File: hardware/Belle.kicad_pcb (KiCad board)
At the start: 2 copper layers, 44.4 x 44.5 mm, 24 parts, among them P1 Bell CONN, P2 Battery CONN, P3 FTDI Flashing CONN, P4 Boot JUMPER, U1 74AHC1G14, U2 ESP-12, U3 AP2112

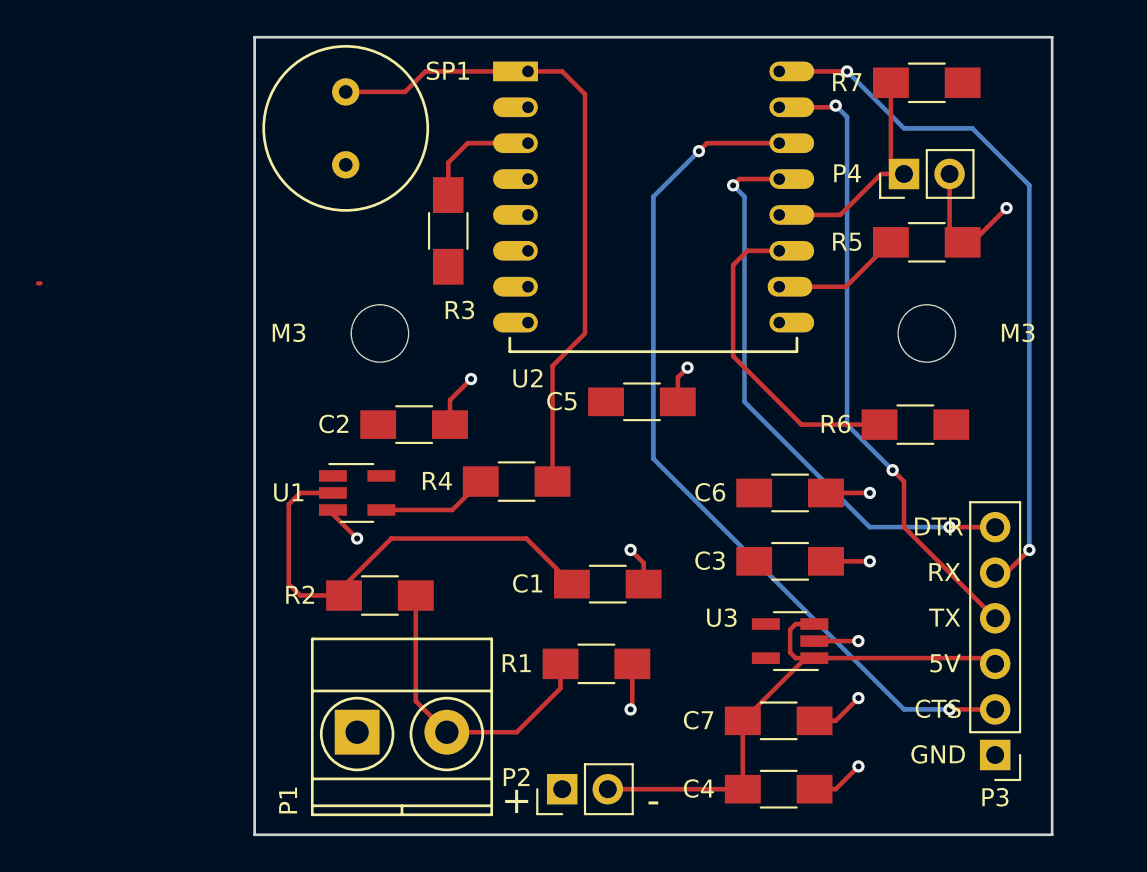
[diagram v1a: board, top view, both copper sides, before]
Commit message: add board info on the silkscreen. close #16
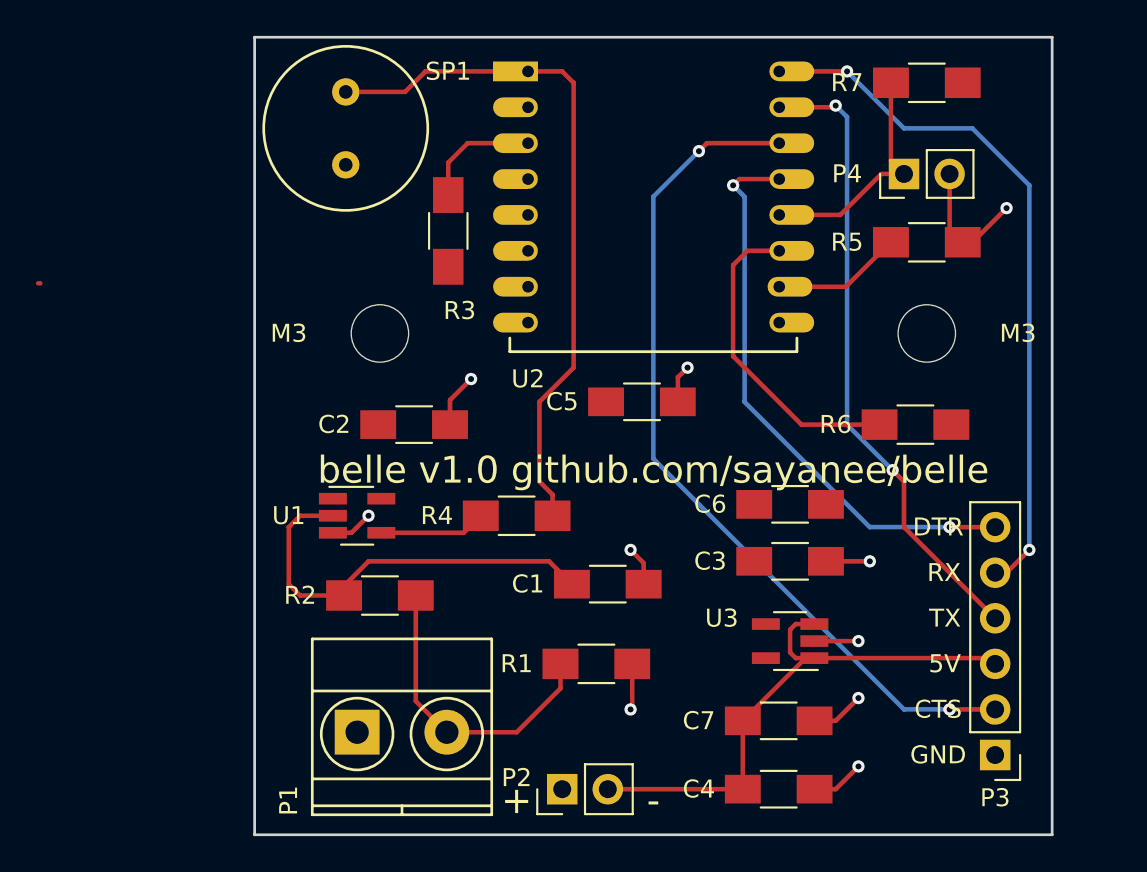
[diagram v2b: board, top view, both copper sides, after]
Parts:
- moved R4 1.91 mm to (167.0, 110.5)
- moved U1 1.27 mm to (158.1, 110.5)
- moved C6 0.64 mm to (182.2, 109.9)
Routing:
- net GND: track 33.5 -> 31.2 mm, vias 11 -> 10
- net Net-(R4-Pad1): track 36.7 -> 38.7 mm
- net Net-(C1-Pad1): track 25.3 -> 23.7 mm
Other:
- board text added: "belle v1.0 github.com/sayanee/belle"
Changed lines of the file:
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@@
   (general
     (links 46)
-    (no_connects 0)
+    (no_connects 1)
     (area 139.955999 76.695999 196.925001 128.345001)
     (thickness 1.6)
-    (drawings 12)
-    (tracks 123)
+    (drawings 13)
+    (tracks 124)
     (zones 0)
     (modules 24)
@@
   (layers
     (0 F.Cu signal)
-    (31 B.Cu signal)
+    (31 B.Cu signal hide)
     (32 B.Adhes user)
     (33 F.Adhes user)
@@
   )
   (module Resistors_SMD:R_1206_HandSoldering (layer F.Cu)
-    (at 167.005 108.585 180)
+    (at 167.005 110.49 180)
     (descr "Resistor SMD 1206, hand soldering")
     (tags "resistor 1206")
@@
   )
   (module TO_SOT_Packages_SMD:SOT-23-5_HandSoldering (layer F.Cu)
-    (at 158.115 109.22)
+    (at 158.115 110.49)
     (descr "5-pin SOT23 package")
     (tags "SOT-23-5 hand-soldering")
@@
   )
   (module Capacitors_SMD:C_1206_HandSoldering (layer F.Cu)
-    (at 182.245 109.22)
+    (at 182.245 109.855)
     (descr "Capacitor SMD 1206, hand soldering")
     (tags "capacitor 1206")
@@
     (pad 1 np_thru_hole circle (at 0 0) (size 3.2 3.2) (drill 3.2) (layers *.Cu *.Mask))
   )
+  (gr_text "belle v1.0 github.com/sayanee/belle" (at 174.625 107.95) (layer F.SilkS)
+    (effects (font (size 1.5 1.5) (thickness 0.3)))
+  )
   (gr_text - (at 174.625 126.365) (layer F.SilkS)
     (effects (font (size 1.5 1.5) (thickness 0.3)))
@@
   (gr_line (start 152.4 83.82) (end 196.85 83.82) (angle 90) (layer Edge.Cuts) (width 0.15))
   (segment (start 140.462 97.536) (end 140.335 97.536) (width 0.25) (layer F.Cu) (net 0))
-  (segment (start 156.765 109.22) (end 154.94 109.22) (width 0.254) (layer F.Cu) (net 1))
+  (segment (start 157.385 114.935) (end 157.385 114.395) (width 0.254) (layer F.Cu) (net 1))
+  (segment (start 157.385 114.395) (end 158.75 113.03) (width 0.254) (layer F.Cu) (net 1))
+  (segment (start 168.815 113.03) (end 170.085 114.3) (width 0.254) (layer F.Cu) (net 1))
+  (segment (start 158.75 113.03) (end 168.815 113.03) (width 0.254) (layer F.Cu) (net 1))
+  (segment (start 156.765 110.49) (end 154.94 110.49) (width 0.254) (layer F.Cu) (net 1))
   (segment (start 154.94 114.935) (end 157.385 114.935) (width 0.254) (layer F.Cu) (net 1))
   (segment (start 154.305 114.3) (end 154.94 114.935) (width 0.254) (layer F.Cu) (net 1))
-  (segment (start 154.305 109.855) (end 154.305 114.3) (width 0.254) (layer F.Cu) (net 1))
-  (segment (start 154.94 109.22) (end 154.305 109.855) (width 0.254) (layer F.Cu) (net 1))
+  (segment (start 154.305 111.125) (end 154.305 114.3) (width 0.254) (layer F.Cu) (net 1))
+  (segment (start 154.94 110.49) (end 154.305 111.125) (width 0.254) (layer F.Cu) (net 1))
   (segment (start 157.385 114.3) (end 157.48 114.3) (width 0.254) (layer F.Cu) (net 1))
-  (segment (start 157.48 114.3) (end 160.02 111.76) (width 0.254) (layer F.Cu) (net 1))
-  (segment (start 167.545 111.76) (end 170.085 114.3) (width 0.254) (layer F.Cu) (net 1))
-  (segment (start 160.02 111.76) (end 167.545 111.76) (width 0.254) (layer F.Cu) (net 1))
+  (segment (start 156.765 111.44) (end 157.8 111.44) (width 0.254) (layer F.Cu) (net 2))
+  (via (at 158.75 110.49) (size 0.6858) (drill 0.3302) (layers F.Cu B.Cu) (net 2))
+  (segment (start 157.8 111.44) (end 158.75 110.49) (width 0.254) (layer F.Cu) (net 2))
   (segment (start 191.865 95.25) (end 192.405 95.25) (width 0.254) (layer F.Cu) (net 2))
   (segment (start 192.405 95.25) (end 194.31 93.345) (width 0.254) (layer F.Cu) (net 2))
@@
   (segment (start 183.595 117.475) (end 186.055 117.475) (width 0.254) (layer F.Cu) (net 2))
   (via (at 186.055 117.475) (size 0.6858) (drill 0.3302) (layers F.Cu B.Cu) (net 2))
-  (segment (start 184.245 109.22) (end 186.69 109.22) (width 0.254) (layer F.Cu) (net 2))
-  (via (at 186.69 109.22) (size 0.6858) (drill 0.3302) (layers F.Cu B.Cu) (net 2))
   (segment (start 184.245 113.03) (end 186.69 113.03) (width 0.254) (layer F.Cu) (net 2))
   (via (at 186.69 113.03) (size 0.6858) (drill 0.3302) (layers F.Cu B.Cu) (net 2))
-  (segment (start 156.765 110.17) (end 156.765 110.41) (width 0.254) (layer F.Cu) (net 2))
-  (segment (start 156.765 110.41) (end 158.115 111.76) (width 0.254) (layer F.Cu) (net 2))
-  (via (at 158.115 111.76) (size 0.6858) (drill 0.3302) (layers F.Cu B.Cu) (net 2))
   (segment (start 161.385 114.935) (end 161.385 120.825) (width 0.254) (layer F.Cu) (net 3))
   (segment (start 161.385 120.825) (end 163.115 122.555) (width 0.254) (layer F.Cu) (net 3))
@@
   (segment (start 163.195 90.805) (end 164.275 89.725) (width 0.254) (layer F.Cu) (net 8))
   (segment (start 167.64 85.725) (end 169.545 85.725) (width 0.254) (layer F.Cu) (net 9))
-  (segment (start 169.005 102.14) (end 169.005 108.585) (width 0.254) (layer F.Cu) (net 9))
-  (segment (start 170.815 100.33) (end 169.005 102.14) (width 0.254) (layer F.Cu) (net 9))
-  (segment (start 170.815 86.995) (end 170.815 100.33) (width 0.254) (layer F.Cu) (net 9))
-  (segment (start 169.545 85.725) (end 170.815 86.995) (width 0.254) (layer F.Cu) (net 9))
+  (segment (start 169.005 109.315) (end 169.005 110.49) (width 0.254) (layer F.Cu) (net 9))
+  (segment (start 168.275 108.585) (end 169.005 109.315) (width 0.254) (layer F.Cu) (net 9))
+  (segment (start 168.275 104.14) (end 168.275 108.585) (width 0.254) (layer F.Cu) (net 9))
+  (segment (start 170.18 102.235) (end 168.275 104.14) (width 0.254) (layer F.Cu) (net 9))
+  (segment (start 170.18 86.36) (end 170.18 102.235) (width 0.254) (layer F.Cu) (net 9))
+  (segment (start 169.545 85.725) (end 170.18 86.36) (width 0.254) (layer F.Cu) (net 9))
   (segment (start 157.48 86.868) (end 160.782 86.868) (width 0.254) (layer F.Cu) (net 9))
   (segment (start 161.925 85.725) (end 167.64 85.725) (width 0.254) (layer F.Cu) (net 9))
@@
   (segment (start 185.04 93.725) (end 181.64 93.725) (width 0.254) (layer F.Cu) (net 18))
   (segment (start 187.325 91.44) (end 185.04 93.725) (width 0.254) (layer F.Cu) (net 18))
-  (segment (start 159.465 110.17) (end 163.42 110.17) (width 0.254) (layer F.Cu) (net 19))
-  (segment (start 163.42 110.17) (end 165.005 108.585) (width 0.254) (layer F.Cu) (net 19))
+  (segment (start 159.465 111.44) (end 164.055 111.44) (width 0.254) (layer F.Cu) (net 19))
+  (segment (start 164.055 111.44) (end 165.005 110.49) (width 0.254) (layer F.Cu) (net 19))
   (segment (start 181.64 97.725) (end 185.355 97.725) (width 0.254) (layer F.Cu) (net 20))
   (segment (start 185.355 97.725) (end 187.83 95.25) (width 0.254) (layer F.Cu) (net 20))

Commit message: add dfm tweaks. #18
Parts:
- added R8: 0R, Resistors_SMD:R_1206_HandSoldering, F.Cu at (178.4, 115.6)
- moved R3 4.49 mm to (158.8, 95.2), turned to 180 degrees
- moved U3 3.81 mm to (186.1, 117.5)
- moved C3 3.24 mm to (185.4, 113.7)
- moved C6 1.91 mm to (184.2, 109.9)
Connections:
- U3 pad 5: +3V3 -> Net-(R8-Pad1)
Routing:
- net Net-(R8-Pad1): track 0.00 -> 6.62 mm
- net /TX: track 35.4 -> 41.6 mm
- net Net-(R3-Pad1): track 6.70 -> 9.18 mm
- net GND: track 31.2 -> 32.4 mm, vias 10 -> 11
- net /5V: track 31.3 -> 32.5 mm
